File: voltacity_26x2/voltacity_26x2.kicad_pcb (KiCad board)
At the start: 2 copper layers, 322.6 x 124.4 mm, 89 parts, among them J1 2-Pin JST, J2 2-Pin JST, J4 78127-1128, SW1 Switch

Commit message: Fixed the incorrect footprints for Kailh Choc hot-swap sockets
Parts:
- added H1: MountingHole, MountingHole:MountingHole_2.2mm_M2_Pad_TopBottom, F.Cu at (234.2, 124.5)
- added H1: MountingHole, MountingHole:MountingHole_2.2mm_M2_Pad_TopBottom, B.Cu at (191.6, 124.5)
- added H2: MountingHole, MountingHole:MountingHole_2.2mm_M2_Pad_TopBottom, F.Cu at (254.9, 161.8)
- added H2: MountingHole, MountingHole:MountingHole_2.2mm_M2_Pad_TopBottom, B.Cu at (170.9, 161.8)
- added H3: MountingHole, MountingHole:MountingHole_2.2mm_M2_Pad_TopBottom, F.Cu at (277.8, 115.7)
- added H3: MountingHole, MountingHole:MountingHole_2.2mm_M2_Pad_TopBottom, B.Cu at (148.0, 115.7)
- added H4: MountingHole, MountingHole:MountingHole_2.2mm_M2_Pad_TopBottom, F.Cu at (314.0, 169.1)
- added H4: MountingHole, MountingHole:MountingHole_2.2mm_M2_Pad_TopBottom, B.Cu at (111.8, 169.1)
- added H5: MountingHole, MountingHole:MountingHole_2.2mm_M2_Pad_TopBottom, F.Cu at (314.9, 139.3)
- added H5: MountingHole, MountingHole:MountingHole_2.2mm_M2_Pad_TopBottom, B.Cu at (110.9, 139.3)
- added H6: MountingHole, MountingHole:MountingHole_2.2mm_M2_Pad_TopBottom, F.Cu at (347.5, 200.3)
- added H6: MountingHole, MountingHole:MountingHole_2.2mm_M2_Pad_TopBottom, B.Cu at (78.3, 200.3)
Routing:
- net Col_3: track 262.6 -> 265.4 mm
- net Row_3: track 238.5 -> 237.7 mm
- removed copper zone on B.Cu, net GND
- removed copper zone on F.Cu, net GND
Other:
- outline, holes or cut-outs redrawn

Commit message: Added new mounting holes
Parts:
- removed the H1 at (234.2, 124.5)
- removed the H1 at (191.6, 124.5)
- removed the H2 at (254.9, 161.8)
- removed the H2 at (170.9, 161.8)
- removed the H3 at (277.8, 115.7)
- removed the H3 at (148.0, 115.7)
- removed the H4 at (314.0, 169.1)
- removed the H4 at (111.8, 169.1)
- removed the H5 at (314.9, 139.3)
- removed the H5 at (110.9, 139.3)
- removed the H6 at (347.5, 200.3)
- removed the H6 at (78.3, 200.3)
- added ?: , , F.Cu at (228.8, 150.5)
- added ?: , , F.Cu at (224.7, 159.8)
- added ?: , , F.Cu at (273.6, 124.0)
- added ?: , , F.Cu at (234.9, 113.9)
- added ?: , , F.Cu at (230.7, 150.5)
- added ?: , , F.Cu at (341.6, 199.7)
- added ?: , , F.Cu at (352.5, 193.5)
- added ?: , , F.Cu at (354.6, 190.5)
- added ?: , , F.Cu at (252.9, 113.0)
- added ?: , , B.Cu at (93.3, 169.6)
- added ?: , , B.Cu at (77.9, 201.3)
- added ?: , , F.Cu at (251.1, 113.0)
- added ?: , , B.Cu at (169.7, 162.7)
- added ?: , , B.Cu at (191.5, 118.6)
- added ?: , , B.Cu at (131.6, 165.1)
- added ?: , , B.Cu at (129.2, 130.7)
- added ?: , , F.Cu at (353.0, 189.6)
- added ?: , , F.Cu at (297.3, 123.5)
- added ?: , , F.Cu at (343.2, 200.6)
- added ?: , , F.Cu at (299.2, 123.5)
- added ?: , , F.Cu at (350.9, 192.6)
- added ?: , , F.Cu at (283.9, 149.0)
- added ?: , , F.Cu at (275.4, 124.0)
- added D1: Diode, Diode_SMD:D_0805_2012Metric, B.Cu at (234.0, 113.9)
- added D10: Diode, Diode_SMD:D_0805_2012Metric, B.Cu at (298.2, 123.5)
- added D11: Diode, Diode_SMD:D_0805_2012Metric, B.Cu at (316.9, 129.0)
- added D12: Diode, Diode_SMD:D_0805_2012Metric, B.Cu at (333.5, 133.0)
- added D13: Diode, Diode_SMD:D_0805_2012Metric, B.Cu at (229.7, 150.5)
- added D14: Diode, Diode_SMD:D_0805_2012Metric, B.Cu at (249.8, 150.3)
- added D15: Diode, Diode_SMD:D_0805_2012Metric, B.Cu at (272.0, 143.3)
- added D16: Diode, Diode_SMD:D_0805_2012Metric, B.Cu at (295.5, 142.5)
- added D17: Diode, Diode_SMD:D_0805_2012Metric, B.Cu at (312.2, 146.0)
- added D18: Diode, Diode_SMD:D_0805_2012Metric, B.Cu at (329.9, 151.5)
- added D19: Diode, Diode_SMD:D_0805_2012Metric, B.Cu at (270.0, 162.8)
- added D2: Diode, Diode_SMD:D_0805_2012Metric, B.Cu at (252.0, 113.0)
- added D20: Diode, Diode_SMD:D_0805_2012Metric, B.Cu at (288.5, 161.8)
- added D21: Diode, Diode_SMD:D_0805_2012Metric, B.Cu at (308.5, 166.3)
- added D22: Diode, Diode_SMD:D_0805_2012Metric, B.Cu at (322.9, 170.5)
- added D23: Diode, Diode_SMD:D_0805_2012Metric, B.Cu at (353.8, 190.0)
- added D24: Diode, Diode_SMD:D_0805_2012Metric, B.Cu at (351.7, 193.1)
- added D25: Diode, Diode_SMD:D_0805_2012Metric, B.Cu at (341.0, 202.6)
- added D26: Diode, Diode_SMD:D_0805_2012Metric, B.Cu at (342.4, 200.2)
- added D3: Diode, Diode_SMD:D_0805_2012Metric, B.Cu at (276.8, 105.2)
- added D4: Diode, Diode_SMD:D_0805_2012Metric, B.Cu at (301.0, 108.3)
- added D5: Diode, Diode_SMD:D_0805_2012Metric, B.Cu at (318.6, 116.8)
- added D6: Diode, Diode_SMD:D_0805_2012Metric, B.Cu at (338.2, 118.3)
- added D7: Diode, Diode_SMD:D_0805_2012Metric, B.Cu at (232.2, 131.5)
- added D8: Diode, Diode_SMD:D_0805_2012Metric, B.Cu at (251.0, 131.5)
- added D9: Diode, Diode_SMD:D_0805_2012Metric, B.Cu at (274.5, 124.0)
- added H1: MountingHole, MountingHole:MountingHole_2.2mm_M2_Pad_TopBottom, F.Cu at (234.2, 118.6)
- added H10: MountingHole, MountingHole:MountingHole_2.2mm_M2_Pad_TopBottom, F.Cu at (298.3, 74.2)
- added H11: MountingHole, MountingHole:MountingHole_2.2mm_M2_Pad_TopBottom, F.Cu at (298.3, 80.1)
- added H12: MountingHole, MountingHole:MountingHole_2.2mm_M2_Pad_TopBottom, F.Cu at (298.3, 86.1)
- added H13: MountingHole, MountingHole:MountingHole_2.2mm_M2_Pad_TopBottom, F.Cu at (304.2, 74.2)
- added H14: MountingHole, MountingHole:MountingHole_2.2mm_M2_Pad_TopBottom, F.Cu at (304.2, 80.1)
- added H15: MountingHole, MountingHole:MountingHole_2.2mm_M2_Pad_TopBottom, F.Cu at (304.2, 86.1)
- added H2: MountingHole, MountingHole:MountingHole_2.2mm_M2_Pad_TopBottom, F.Cu at (256.1, 162.7)
- added H3: MountingHole, MountingHole:MountingHole_2.2mm_M2_Pad_TopBottom, F.Cu at (296.6, 130.7)
- added H4: MountingHole, MountingHole:MountingHole_2.2mm_M2_Pad_TopBottom, F.Cu at (294.1, 165.1)
- added H5: MountingHole, MountingHole:MountingHole_2.2mm_M2_Pad_TopBottom, F.Cu at (347.9, 201.2)
- added H6: MountingHole, MountingHole:MountingHole_2.2mm_M2_Pad_TopBottom, F.Cu at (332.4, 169.6)
- added H7: MountingHole, MountingHole:MountingHole_2.2mm_M2_Pad_TopBottom, F.Cu at (292.3, 74.2)
- added H8: MountingHole, MountingHole:MountingHole_2.2mm_M2_Pad_TopBottom, F.Cu at (292.3, 80.1)
- added H9: MountingHole, MountingHole:MountingHole_2.2mm_M2_Pad_TopBottom, F.Cu at (292.3, 86.1)
- added S1: Keyswitch, Library:SW_choc_v1_HS_CPG135001S30_1u_CHAMFER, B.Cu at (224.7, 121.8)
- added S10: Keyswitch, Library:SW_choc_v1_HS_CPG135001S30_1u_CHAMFER, B.Cu at (286.6, 130.1)
- added S11: Keyswitch, Library:SW_choc_v1_HS_CPG135001S30_1u_CHAMFER, B.Cu at (305.6, 135.9)
- added S12: Keyswitch, Library:SW_choc_v1_HS_CPG135001S30_1u_CHAMFER, B.Cu at (324.7, 140.9)
- added S13: Keyswitch, Library:SW_choc_v1_HS_CPG135001S30_1u_CHAMFER, B.Cu at (224.7, 159.8)
- added S14: Keyswitch, Library:SW_choc_v1_HS_CPG135001S30_1u_CHAMFER, B.Cu at (243.7, 159.8)
- added S15: Keyswitch, Library:SW_choc_v1_HS_CPG135001S30_1u_CHAMFER, B.Cu at (263.3, 151.6)
- added S16: Keyswitch, Library:SW_choc_v1_HS_CPG135001S30_1u_CHAMFER, B.Cu at (283.9, 149.0)
- added S17: Keyswitch, Library:SW_choc_v1_HS_CPG135001S30_1u_CHAMFER, B.Cu at (302.7, 154.6)
- added S18: Keyswitch, Library:SW_choc_v1_HS_CPG135001S30_1u_CHAMFER, B.Cu at (321.4, 159.6)
- added S19: Keyswitch, Library:SW_choc_v1_HS_CPG135001S30_1u_CHAMFER, B.Cu at (264.8, 172.8)
- added S2: Keyswitch, Library:SW_choc_v1_HS_CPG135001S30_1u_CHAMFER, B.Cu at (243.7, 121.8)
- added S20: Keyswitch, Library:SW_choc_v1_HS_CPG135001S30_1u_CHAMFER, B.Cu at (283.9, 172.1)
- added S21: Keyswitch, Library:SW_choc_v1_HS_CPG135001S30_1u_CHAMFER, B.Cu at (302.5, 177.1)
- added S22: Keyswitch, Library:SW_choc_v1_HS_CPG135001S30_1u_CHAMFER, B.Cu at (322.2, 180.9)
- added S23: Keyswitch, Library:SW_choc_v1_HS_CPG135001S30_1u_CHAMFER, B.Cu at (341.8, 188.0)
- added S24: Keyswitch, Library:SW_choc_v1_HS_CPG135001S30_1u_CHAMFER, B.Cu at (359.9, 198.4)
- added S25: Keyswitch, Library:SW_choc_v1_HS_CPG135001S30_1u_CHAMFER, B.Cu at (328.2, 203.9)
- added S26: Keyswitch, Library:SW_choc_v1_HS_CPG135001S30_1u_CHAMFER, B.Cu at (347.0, 213.5)
- added S3: Keyswitch, Library:SW_choc_v1_HS_CPG135001S30_1u_CHAMFER, B.Cu at (266.0, 113.7)
- added S4: Keyswitch, Library:SW_choc_v1_HS_CPG135001S30_1u_CHAMFER, B.Cu at (289.2, 111.3)
- added S5: Keyswitch, Library:SW_choc_v1_HS_CPG135001S30_1u_CHAMFER, B.Cu at (308.6, 117.1)
- added S6: Keyswitch, Library:SW_choc_v1_HS_CPG135001S30_1u_CHAMFER, B.Cu at (328.0, 122.2)
- added S7: Keyswitch, Library:SW_choc_v1_HS_CPG135001S30_1u_CHAMFER, B.Cu at (224.7, 140.8)
- added S8: Keyswitch, Library:SW_choc_v1_HS_CPG135001S30_1u_CHAMFER, B.Cu at (243.7, 140.8)
- added S9: Keyswitch, Library:SW_choc_v1_HS_CPG135001S30_1u_CHAMFER, B.Cu at (264.6, 132.7)
- J4: moved to F.Cu
- S1, S10, S11, S12, S13, S14, S15, S16, S17, S18, S19, S2, S20, S21, S22, S23, S24, S25, S26, S3, S4, S5, S6, S7, S8, S9: footprint Kailh Sockets:REVERSED_Kailh_socket_PG1350_reversible -> Library:SW_choc_v1_HS_CPG135001S30_1u_CHAMFER
- moved J4 9.92 mm to (348.9, 167.2), turned to 180 degrees
- moved D26 9.68 mm to (342.4, 200.2)
- moved D6 7.76 mm to (338.2, 118.3)
- moved D23 4.81 mm to (353.8, 190.0)
- moved D5 4.81 mm to (318.6, 116.8), turned to -15 degrees
- moved D25 2.91 mm to (341.0, 202.6)
- moved D24 2.63 mm to (351.7, 193.1)
- moved D4 1.60 mm to (301.0, 108.3)
- moved D3 0.94 mm to (276.8, 105.2)
- moved D1 0.66 mm to (234.0, 113.9)
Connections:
- GPIO1 pad 19: GPIO_INTA -> GPIO_INTB
- GPIO1 pad 20: GPIO_INTB -> GPIO_INTA
- GPIO1 pad 21: TP_BTN1 -> TP_BTN3
- GPIO1 pad 23: TP_BTN3 -> TP_BTN1
- MCU1 pad 18: GPIO_INTA -> GPIO_INTB
- MCU1 pad 19: GPIO_INTB -> GPIO_INTA
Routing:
- net Col_6: track 179.6 -> 301.7 mm, vias 8 -> 6
- net Col_5: track 192.8 -> 284.2 mm, vias 7 -> 4
- net Col_4: track 201.0 -> 264.5 mm, vias 8 -> 4
- net Col_7: track 123.3 -> 173.0 mm
- net Row_4: track 212.8 -> 243.4 mm, vias 8 -> 5
- net TP_BTN3: track 67.2 -> 38.3 mm
- net RESET: track 74.4 -> 46.7 mm
- net GPIO_RESET: track 66.5 -> 45.2 mm, vias 3 -> 2
- net +BATT: track 82.4 -> 63.8 mm, vias 1 -> 2
- net GPIO_INTA: track 34.4 -> 17.2 mm, vias 2 -> 0
- net Col_1: track 286.9 -> 304.0 mm, vias 6 -> 4
- net MISO: track 22.0 -> 36.8 mm, vias 2 -> 1
- net Col_2: track 259.2 -> 273.5 mm, vias 7 -> 6
- net GND: track 171.0 -> 161.0 mm, vias 7 -> 0
- net Row_3: track 237.7 -> 228.2 mm
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- added copper zone on B.Cu, net GND
- added copper zone on F.Cu, net GND
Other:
- board text added: "${REFERENCE}"
- board text added: "${VALUE}"

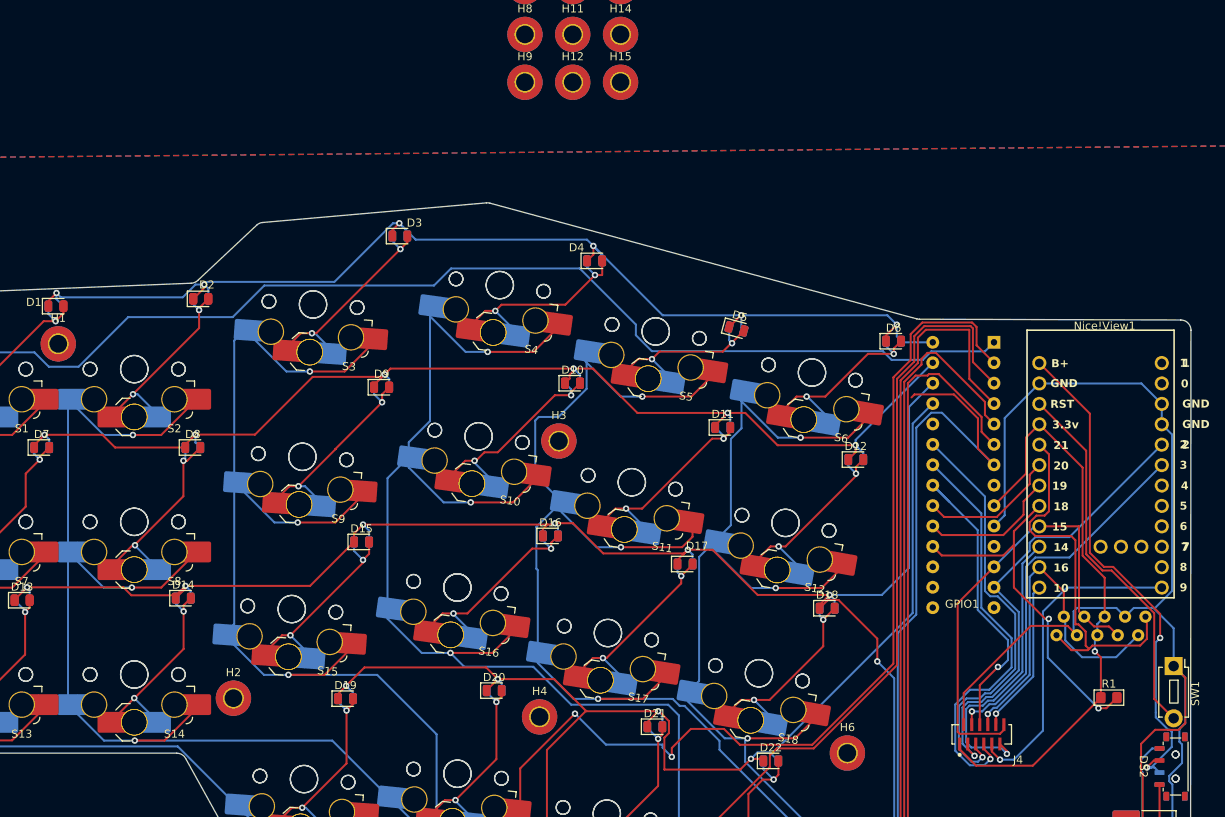
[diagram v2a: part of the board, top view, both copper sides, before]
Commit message: Updated schematic and cleaned up some options
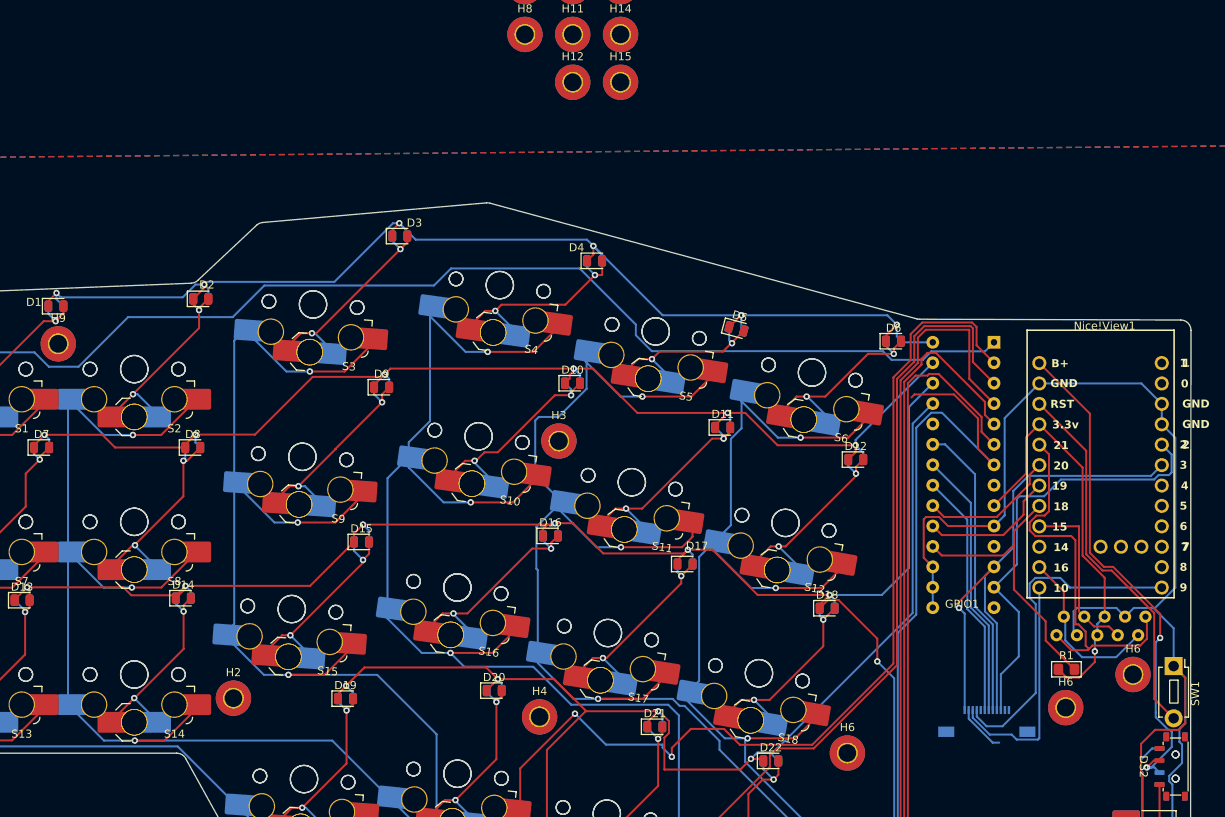
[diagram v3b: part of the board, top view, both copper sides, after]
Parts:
- removed H1: MountingHole, MountingHole:MountingHole_2.2mm_M2_Pad_TopBottom
- removed J4: 78127-1128, Kicad Footprints:Molex-78127-1128-Manufacturer_Recommended
- added H6: MountingHole, MountingHole:MountingHole_2.2mm_M2_Pad_TopBottom, F.Cu at (368.0, 159.8)
- added H6: MountingHole, MountingHole:MountingHole_2.2mm_M2_Pad_TopBottom, F.Cu at (359.6, 163.9)
- added J5: 78127-1128, Kicad Footprints:CON_5051101297_MOL, B.Cu at (349.8, 166.7)
- moved H9 66.6 mm to (234.2, 118.6)
- moved R1 6.35 mm to (359.7, 159.1)
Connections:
- GPIO1 pad 12: SCK -> SCL
- GPIO1 pad 15: unconnected-(GPIO1-A0-Pad15) -> GND
- GPIO1 pad 16: unconnected-(GPIO1-A1-Pad16) -> GND
- GPIO1 pad 17: unconnected-(GPIO1-A2-Pad17) -> GND
- GPIO1 pad 18: GPIO_RESET -> VCC
- GPIO1 pad 19: GPIO_INTB -> unconnected-(GPIO1-INTB-Pad19)
- GPIO1 pad 21: TP_BTN3 -> TP_BTN2
- GPIO1 pad 22: TP_BTN2 -> TP_BTN3
- MCU1 pad 17: GPIO_RESET -> unconnected-(MCU1-18-Pad17)
- MCU1 pad 18: GPIO_INTB -> unconnected-(MCU1-19-Pad18)
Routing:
- net MISO: track 36.8 -> 6.31 mm, vias 1 -> 0
- net MOSI: track 44.7 -> 22.2 mm, vias 1 -> 0
- net VCC: track 73.2 -> 51.7 mm
- net TP_BTN2: track 51.6 -> 30.7 mm, vias 1 -> 0
- net GPIO_INTB: track 17.3 -> 0.00 mm
- net (no net): track 0.00 -> 17.3 mm
- net SCK: track 58.4 -> 42.2 mm, vias 0 -> 1
- net TP_BTN1: track 52.8 -> 37.1 mm, vias 1 -> 0
- net SS: track 19.3 -> 29.2 mm, vias 1 -> 0
- net GPIO_RESET: track 45.2 -> 35.9 mm, vias 2 -> 0
- net TP_BTN3: track 38.3 -> 33.4 mm, vias 1 -> 0
- net SDA: track 57.9 -> 54.2 mm, vias 1 -> 0
- net SCL: track 45.8 -> 48.7 mm, vias 1 -> 0
- net DR: track 40.0 -> 41.5 mm, vias 1 -> 0
- net GND: track 161.0 -> 160.1 mm

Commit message: Added .blend of case & plate
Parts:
- removed the ? at (234.9, 113.9)
- removed the ? at (341.6, 199.7)
- removed the ? at (352.5, 193.5)
- removed the ? at (354.6, 190.5)
- removed the ? at (93.3, 169.6)
- removed the ? at (77.9, 201.3)
- removed the ? at (169.7, 162.7)
- removed the ? at (191.5, 118.6)
- removed the ? at (131.6, 165.1)
- removed the ? at (129.2, 130.7)
- removed the ? at (353.0, 189.6)
- removed the ? at (343.2, 200.6)
- removed the ? at (299.2, 123.5)
- removed the ? at (350.9, 192.6)
- removed DS2: SW_DIP_x01, ScottoKeebs_Components:Switch_MSK12C02
- removed H10, H11, H12, H13, H14, H15, H7, H8: MountingHole, MountingHole:MountingHole_2.2mm_M2_Pad_TopBottom
- removed the H6 at (368.0, 159.8)
- removed the H6 at (359.6, 163.9)
- removed J2: 2-Pin JST, Connector_JST:JST_PH_S2B-PH-SM4-TB_1x02-1MP_P2.00mm_Horizontal
- removed J5: 78127-1128, Kicad Footprints:CON_5051101297_MOL
- removed R1: R_0805, PCM_Resistor_SMD_AKL:R_0805_2012Metric_Pad1.20x1.40mm_HandSolder
- removed the S22 at (322.2, 180.9)
- removed the S22 at (103.5, 180.9)
- added H2: MountingHole, MountingHole:MountingHole_2.2mm_M2_Pad_TopBottom, B.Cu at (169.4, 162.7)
- added H3: MountingHole, MountingHole:MountingHole_2.2mm_M2_Pad_TopBottom, B.Cu at (128.9, 130.7)
- added H4: MountingHole, MountingHole:MountingHole_2.2mm_M2_Pad_TopBottom, B.Cu at (131.3, 165.0)
- added H5: MountingHole, MountingHole:MountingHole_2.2mm_M2_Pad_TopBottom, B.Cu at (77.6, 201.2)
- added H6: MountingHole, MountingHole:MountingHole_2.2mm_M2_Pad_TopBottom, B.Cu at (93.0, 169.5)
- added H9: MountingHole, MountingHole:MountingHole_2.2mm_M2_Pad_TopBottom, B.Cu at (170.5, 121.7)
- added J4: 78127-1128, Kicad Footprints:CON_5051101297_MOL, F.Cu at (348.5, 163.7)
- added REF**: Breakoff, Library:Breakoff, F.Cu at (234.2, 117.6)
- added REF**: Breakoff, Library:Breakoff, F.Cu at (234.2, 151.7)
- added REF**: Breakoff, Library:Breakoff, F.Cu at (235.5, 157.1)
- added REF**: Breakoff, Library:Breakoff, F.Cu at (213.4, 171.2)
- added REF**: Breakoff, Library:Breakoff, F.Cu at (235.6, 171.4)
- added REF**: Breakoff, Library:Breakoff, F.Cu at (213.4, 145.4)
- added REF**: Breakoff, Library:Breakoff, B.Cu at (191.4, 157.1)
- added REF**: Breakoff, Library:Breakoff, B.Cu at (213.3, 145.4)
- added REF**: Breakoff, Library:Breakoff, B.Cu at (213.4, 115.3)
- added REF**: Breakoff, Library:Breakoff, B.Cu at (191.4, 151.7)
- added REF**: Breakoff, Library:Breakoff, B.Cu at (213.4, 126.6)
- added REF**: Breakoff, Library:Breakoff, F.Cu at (213.4, 152.3)
- added REF**: Breakoff, Library:Breakoff, B.Cu at (191.4, 137.3)
- added REF**: Breakoff, Library:Breakoff, B.Cu at (191.3, 171.3)
- added REF**: Breakoff, Library:Breakoff, B.Cu at (213.4, 133.6)
- added REF**: Breakoff, Library:Breakoff, B.Cu at (191.4, 132.5)
- added REF**: Breakoff, Library:Breakoff, B.Cu at (191.4, 117.5)
- added REF**: Breakoff, Library:Breakoff, B.Cu at (191.4, 110.4)
- added REF**: Breakoff, Library:Breakoff, B.Cu at (213.3, 164.2)
- added REF**: Breakoff, Library:Breakoff, B.Cu at (213.3, 171.2)
- added REF**: Breakoff, Library:Breakoff, B.Cu at (213.3, 152.3)
- added REF**: Breakoff, Library:Breakoff, F.Cu at (213.4, 164.2)
- added REF**: Breakoff, Library:Breakoff, F.Cu at (213.4, 126.6)
- added REF**: Breakoff, Library:Breakoff, F.Cu at (213.4, 115.3)
- added REF**: Breakoff, Library:Breakoff, F.Cu at (234.3, 132.5)
- added REF**: Breakoff, Library:Breakoff, F.Cu at (234.3, 137.3)
- added REF**: Breakoff, Library:Breakoff, F.Cu at (213.4, 133.6)
- added REF**: Breakoff, Library:Breakoff, F.Cu at (234.2, 110.5)
- added S22: Keyswitch, Library:SW_choc_v1_HS_CPG135001S30_1u_CHAMFER, F.Cu at (323.5, 180.9)
- added S22: Keyswitch, ScottoKeebs_Cutout:Cutout_Choc, B.Cu at (103.3, 180.9)
- added SW2: RotaryEncoder, Rotary_Encoder:RotaryEncoder_Alps_EC12E_Vertical_H20mm, F.Cu at (348.3, 213.5)
- added SW3: RotaryEncoder, Rotary_Encoder:RotaryEncoder_Alps_EC12E_Vertical_H20mm, F.Cu at (361.2, 198.4)
- added SW4: RotaryEncoder, Rotary_Encoder:RotaryEncoder_Alps_EC12E_Vertical_H20mm, F.Cu at (269.2, 165.1)
- S1, S10, S11, S12, S13, S14, S15, S16, S17, S18, S19, S2, S20, S21, S23, S24, S25, S26, S3, S4, S5, S6, S7, S8, S9: footprint ScottoKeebs_Cutout:Cutout_Choc_1.00u -> ScottoKeebs_Cutout:Cutout_Choc
- moved H9 22.3 mm to (256.3, 121.7)
- moved D24 19.7 mm to (371.4, 194.3), turned to 0 degrees
- moved D24 19.7 mm to (371.4, 194.3), turned to 180 degrees
- moved D26 18.2 mm to (358.3, 209.1), turned to 0 degrees
- moved D26 18.2 mm to (358.3, 209.1), turned to 180 degrees
- moved SW1 11.5 mm to (362.3, 162.8), turned to 0 degrees
- moved D23 7.93 mm to (352.6, 182.2), turned to 0 degrees
- moved D23 7.93 mm to (352.6, 182.2), turned to 180 degrees
- moved D25 5.11 mm to (339.1, 197.9), turned to 0 degrees
- moved D25 5.10 mm to (339.1, 197.9), turned to 180 degrees
- moved Nice!View1 4.74 mm to (366.0, 158.3)
- moved D1 3.60 mm to (230.8, 112.1)
- moved D1 3.58 mm to (230.9, 112.1)
- moved ? 1.61 mm to (252.3, 112.1)
- moved ? 1.61 mm to (254.2, 112.1)
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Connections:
- D19 pad 1: Row_4 -> Thu_Row_1 (x2)
- D20 pad 1: Row_4 -> Thu_Row_1 (x2)
- D21 pad 1: Row_4 -> Thu_Row_1 (x2)
- D22 pad 1: Row_4 -> Thu_Row_1 (x2)
- D23 pad 1: Row_4 -> Thu_Row_1 (x2)
- D24 pad 1: Row_4 -> Thu_Row_1 (x2)
- D25 pad 1: Row_3 -> Thu_Row_2 (x2)
- D26 pad 1: Row_4 -> Thu_Row_2 (x2)
- GPIO1 pad 21: TP_BTN2 -> TP_BTN1
- GPIO1 pad 23: TP_BTN1 -> TP_BTN2
- GPIO1 pad 24: unconnected-(GPIO1-GPA3-Pad24) -> Thu_Row_2
- GPIO1 pad 25: Row_4 -> Thu_Row_1
- GPIO1 pad 7: Col_7 -> Thu_Col_1
- GPIO1 pad 8: unconnected-(GPIO1-GPB7-Pad8) -> Thu_Col_2
- MCU1 pad 10: unconnected-(MCU1-7-Pad10) -> ENC3_B
- MCU1 pad 13: SS -> CS
- MCU1 pad 20: CS -> unconnected-(MCU1-21-Pad20)
- MCU1 pad 25: unconnected-(MCU1-1-Pad25) -> ENC1_A
- MCU1 pad 26: unconnected-(MCU1-2-Pad26) -> ENC1_B
- MCU1 pad 7: unconnected-(MCU1-4-Pad7) -> ENC2_A
- MCU1 pad 8: unconnected-(MCU1-5-Pad8) -> ENC2_B
- MCU1 pad 9: unconnected-(MCU1-6-Pad9) -> ENC3_A
- S19 pad 1: Col_1 -> Col_3 (x2)
- S20 pad 1: Col_2 -> Col_4 (x2)
- S21 pad 1: Col_3 -> Col_5 (x2)
- S22 pad 1: Col_4 -> Col_6
- S23 pad 1: Col_5 -> Thu_Col_1 (x2)
- S24 pad 1: Col_6 -> Thu_Col_2 (x2)
- S25 pad 1: Col_7 -> Thu_Col_1 (x2)
- S26 pad 1: Col_7 -> Thu_Col_2 (x2)
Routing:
- net Row_4: track 243.4 -> 0.00 mm, vias 5 -> 0
- net Thu_Row_1: track 0.00 -> 194.3 mm, vias 0 -> 6
- net ENC1_B: track 0.00 -> 179.0 mm, vias 0 -> 2
- net Col_7: track 173.0 -> 0.00 mm, vias 2 -> 0
- net ENC1_A: track 0.00 -> 172.5 mm, vias 0 -> 2
- net Thu_Col_2: track 0.00 -> 135.6 mm, vias 0 -> 2
- net Thu_Row_2: track 0.00 -> 133.6 mm, vias 0 -> 2
- net Thu_Col_1: track 0.00 -> 123.4 mm, vias 0 -> 2
- net Col_6: track 301.7 -> 184.6 mm, vias 6 -> 5
- net GND: track 160.1 -> 48.7 mm
- net ENC3_A: track 0.00 -> 79.6 mm
- net Col_5: track 284.2 -> 206.7 mm
- net ENC3_B: track 0.00 -> 74.4 mm
- net Col_1: track 304.0 -> 233.7 mm, vias 4 -> 3
- net ENC2_A: track 0.00 -> 61.9 mm
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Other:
- board size 322.6 x 124.4 mm -> 323.1 x 125.1 mm
- board text added: "1"
- board text added: "18x17 spacing"
- board text added: "19.05 spacing"
- board text added: "3"
